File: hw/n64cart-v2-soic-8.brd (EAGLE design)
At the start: 99.1 x 50.8 mm, 40 parts, among them IC1 RP2040-QFN56, J1 N64_EDGE, Q1 BSS84, U1 W25Q128JVSIQ, U3 W25Q256JVEIQ_TR

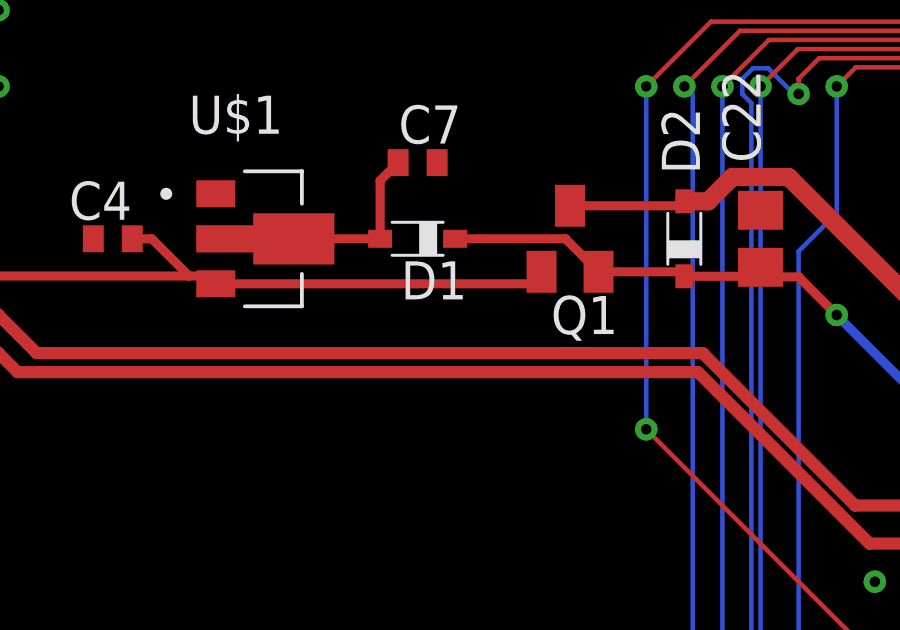
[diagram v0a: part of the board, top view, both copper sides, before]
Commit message: missed pulldown resistor for V2
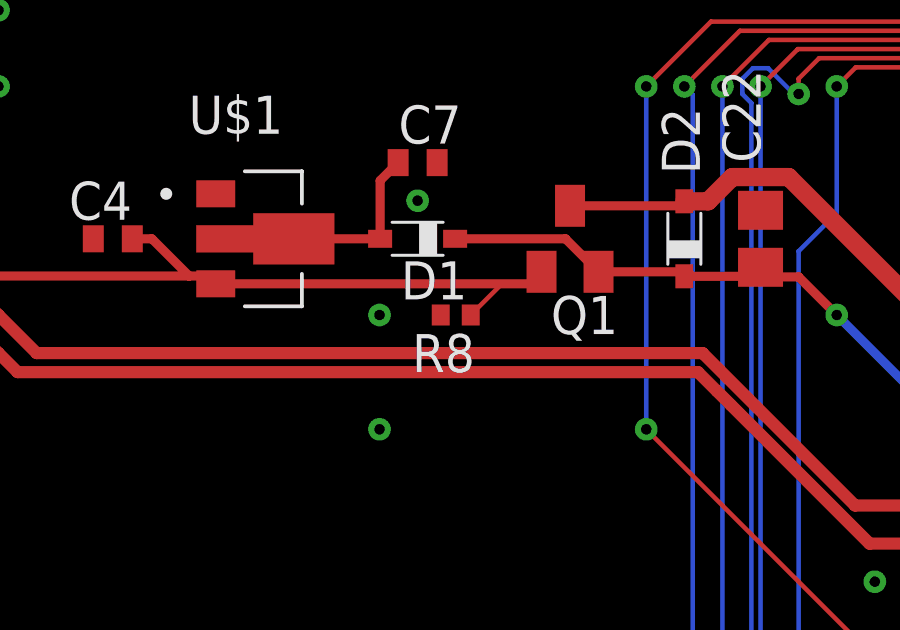
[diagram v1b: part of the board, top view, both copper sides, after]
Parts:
- added R8: 10K, rcl:R0402
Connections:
- net +VBUS: now also R8.1
- net GND: now also R8.2
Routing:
- net +VBUS: track 24.4 -> 26.8 mm
- net GND: vias 136 -> 139
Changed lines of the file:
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@@
 <attribute name="VALUE" x="20.955" y="51.435" size="1.27" layer="27"/>
+</element>
+<element name="R8" library="rcl" library_urn="urn:adsk.eagle:library:334" package="R0402" package3d_urn="urn:adsk.eagle:package:23547/3" value="10K" x="22.86" y="48.26" smashed="yes" rot="R180">
+<attribute name="NAME" x="23.495" y="47.625" size="1.27" layer="25" rot="R180"/>
+<attribute name="POPULARITY" value="0" x="22.86" y="48.26" size="1.778" layer="27" rot="R180" display="off"/>
+<attribute name="SPICEPREFIX" value="R" x="22.86" y="48.26" size="1.778" layer="27" rot="R180" display="off"/>
+<attribute name="VALUE" x="23.495" y="50.165" size="1.27" layer="27" rot="R180"/>
 </element>
 </elements>
@@
 <contactref element="C4" pad="2"/>
 <contactref element="C7" pad="2"/>
+<contactref element="R8" pad="2"/>
+<via x="21.59" y="52.07" extent="1-16" drill="0.35"/>
+<via x="20.32" y="48.26" extent="1-16" drill="0.35"/>
+<via x="20.32" y="44.45" extent="1-16" drill="0.35"/>
 </signal>
 <signal name="+3V3">
@@
 <wire x1="12.08" y1="50.8" x2="12.73" y2="50.8" width="0.3048" layer="1"/>
 <wire x1="12.73" y1="50.8" x2="13.97" y2="49.56" width="0.3048" layer="1"/>
+<contactref element="R8" pad="1"/>
+<wire x1="23.36" y1="48.26" x2="24.4" y2="49.3" width="0.1524" layer="1"/>
+<wire x1="24.4" y1="49.3" x2="25.32" y2="49.3" width="0.1524" layer="1"/>
 </signal>
 <signal name="SWCLK">
